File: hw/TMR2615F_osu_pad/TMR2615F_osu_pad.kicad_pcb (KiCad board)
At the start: 4 copper layers, 70.1 x 60 mm, 167 parts, among them J1 TYPE-C-31-M-12, J2 TYPE-C-31-M-12, J3 TYPE-C-31-M-12, J4 XY-SH1_0-4A61, J5 Conn_01x10, J6 Conn_01x23, J7 Conn_01x06, J8 Conn_01x04, SW1 SKSGPAE010, SW2 SKSGPAE010, SW3 CPG151101S11-16, SW4 CPG151101S11-16, SW5 CPG151101S11-16, SW6 CPG151101S11-16, SW7 CPG151101S11-16, SW8 CPG151101S11-16, U1 SRV05-4A, U10 AT32F405RBT7-7, U11 TMUX1574RSVR, U12 SK6812MINI-E, U13 TMR2615x, U14 SK6812MINI-E, U15 TMR2615x, U16 SK6812MINI-E, U17 TMR2615x, U18 SK6812MINI-E, U19 TMR2615x, U2 LM66100DCK, U20 SK6812MINI-E, U21 TMR2615x, U22 SK6812MINI-E, U23 TMR2615x, U24 SK6812MINI-E, U3 AP22653W6-7, U4 TPS7A4700, U5 SRV05-4A, U6 SRV05-4A, U7 LM66100DCK, U8 XC6206P332MR, U9 SRV05-4A, X1 X322512MSB4SI

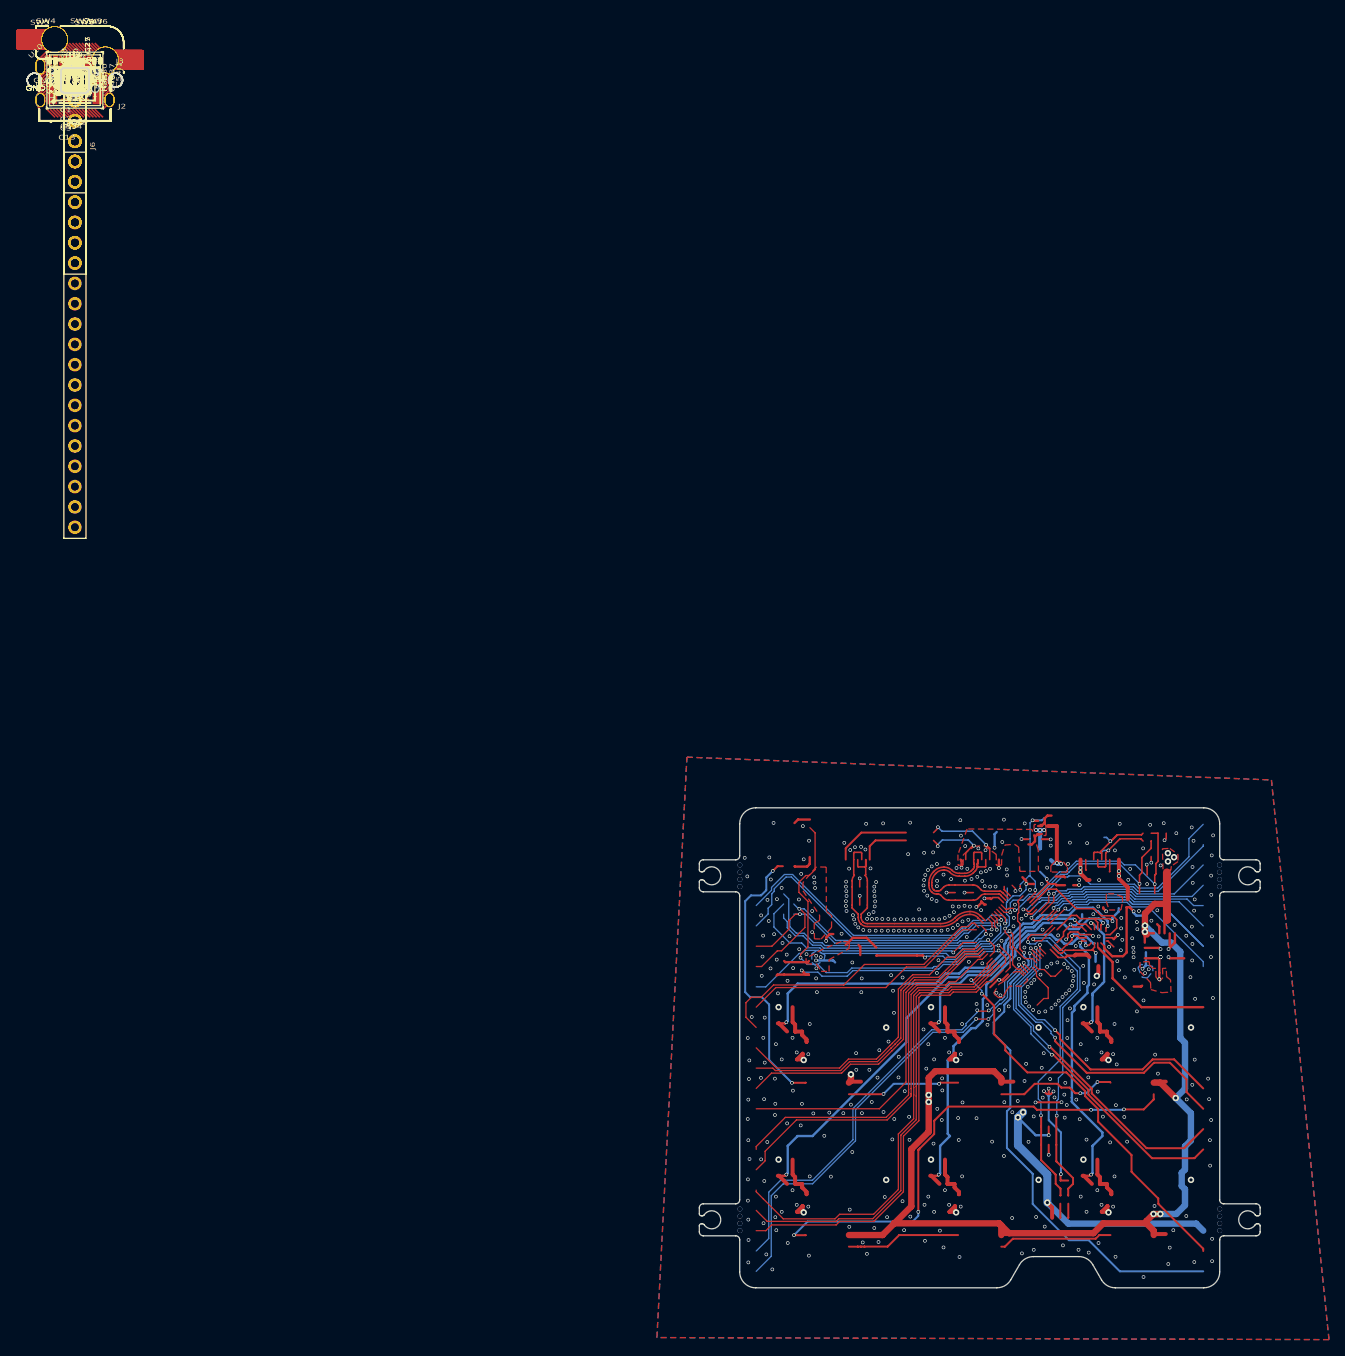
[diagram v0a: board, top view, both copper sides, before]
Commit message: Clear the pre-fab blockers on TMR2615F_osu_pad
All three blockers from prefab_review_2026-08-03.md, plus the should-fix
resistor and a filter retune, in schematic and layout.

U8 XC6206P332MR pinout corrected to the SOT-23 assignment in the LCSC
datasheet — 1=VSS, 2=VOUT, 3=VIN. Pad 2 now carries +3.3V and pad 3 +5V;
before this the +3.3V rail would have come up at ~4.4 V through the pass
device's body diode, past the AT32F405's 4.0 V absolute maximum.

I2C1 SDA and SCL swapped at the MCU so PF4=SDA and PF5=SCL, matching
AT32F405 datasheet Table 9. These pins have no internal remap, so J4's
accessory port had no working hardware I2C before.

U6 (SRV05-4A, SOT-23-6, 3-5 pF per channel and doubled onto each line)
deleted from the USB HS pair and replaced with U25/U26, one
PESD5V0R1BSFYL each on D+ and D-: SOD-962, 0.15 pF, which fits the
~1-2 pF budget at 480 Mbps. The pair was re-dressed around the new
footprints (1789 -> 1766 segments, 628 -> 620 vias). A schematic note
records the fallback: the 0201-class parts can be omitted, or 0402
sub-3 pF diodes fitted on the DNP C17/C18 pads, if assembly balks.

BOOT0 pull-down R26 10 k -> 3.3 k. Table 9 footnote 7 asks for 3.3 kohm
or below.

Sensor and VBUS_B sense filters retuned from 330 ohm + 47 nF to
5.1 kohm + 3.3 nF (R8, R29-R34; C10, C34, C38, C42, C46, C50, C54).
47 nF was over the TMR2615's 10 nF maximum load capacitance; 3.3 nF is
inside it, and the larger series resistor keeps the corner where it was
(tau 16.8 us, f_c 9.46 kHz).

LCSC codes filled in for the three parts the fab BOM could not source
automatically: U2/U7 LM66100DCK = C2869734, U4 TPS7A4700 = C28286.
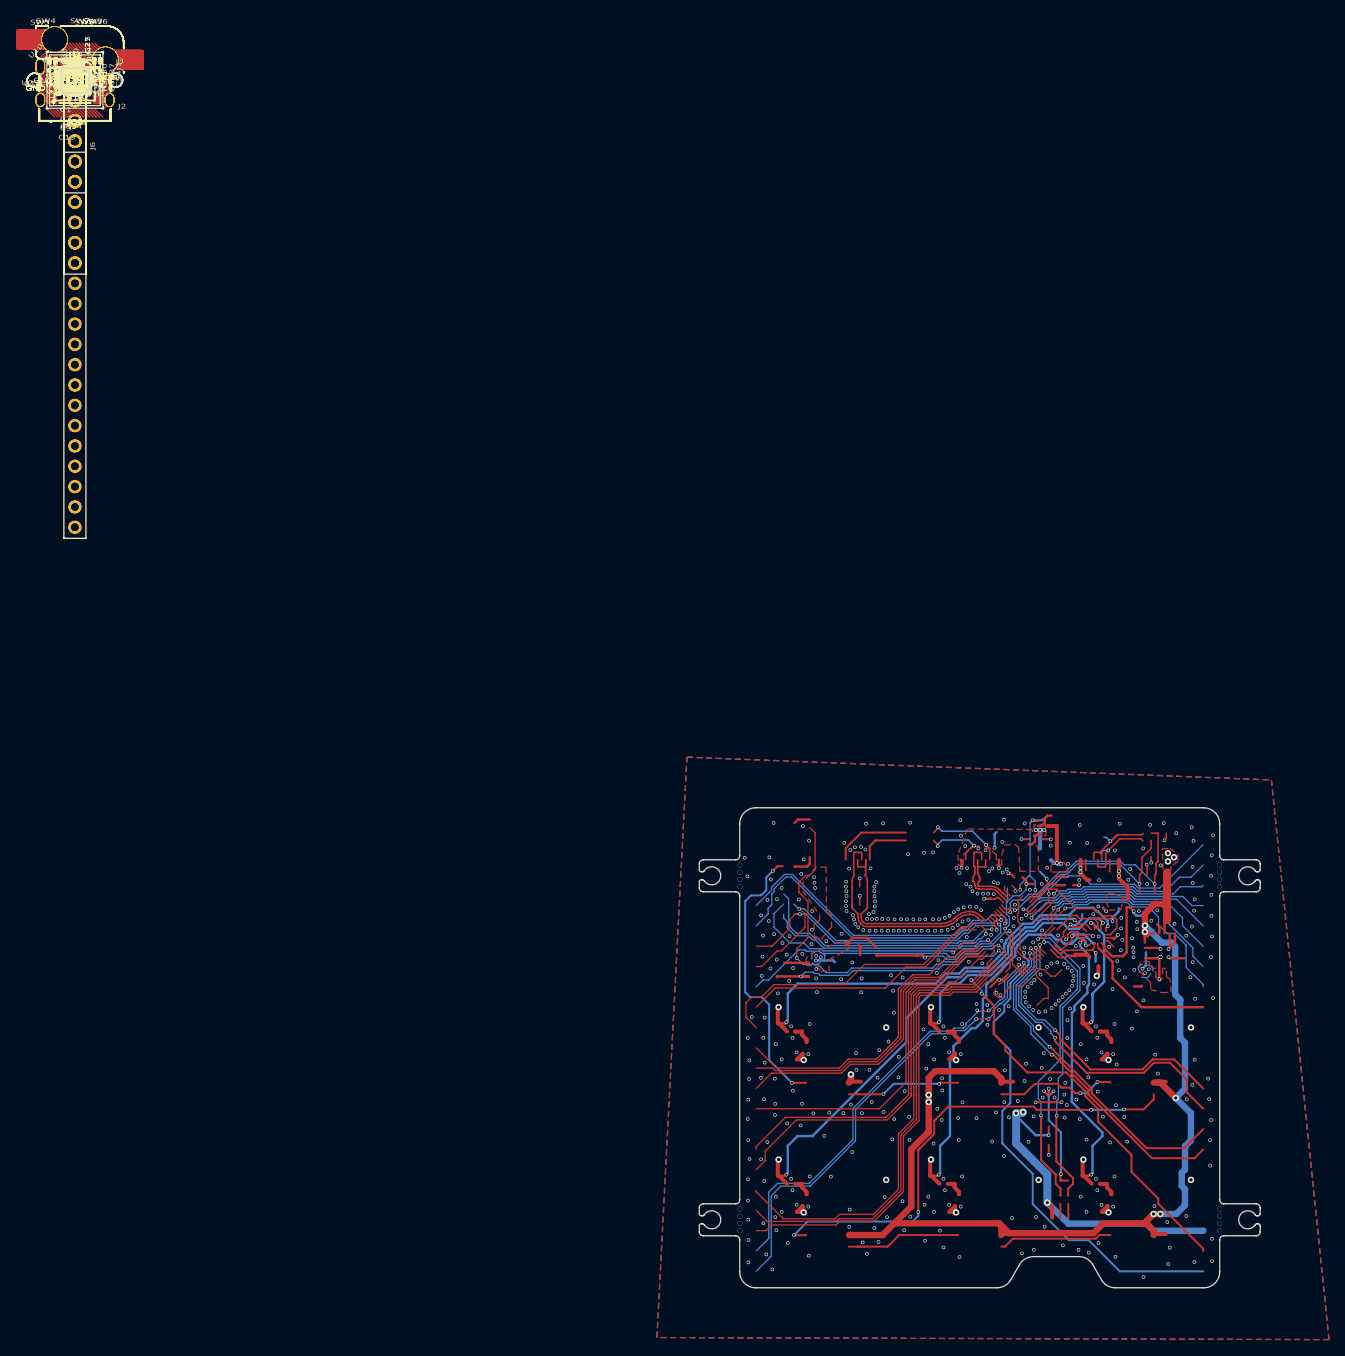
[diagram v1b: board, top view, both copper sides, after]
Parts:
- removed U6: SRV05-4A, Diode__C:SOT-23-6
- added U25, U26: PESD5V0R1BSFYL, Diode__C:SOD-962_L0.6-W0.3-BI, F.Cu at (0.00, 0.00)
- C10, C34, C38, C42, C46, C50, C54: value CL10B473KB8NNNC -> CL10B332KB8NNNC
- R26: value 0402WGF1002TCE -> 0402WGF3301TCE
- R29, R30, R31, R32, R33, R34, R8: value 0402WGF3300TCE -> 0402WGF5101TCE
- U13, U15, U17, U19, U21, U23: value TMR2615x -> TMR2615F-AAC-1.500-500
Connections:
- J5 pad 1: /ADC1_IN15 -> GND
- J5 pad 2: /ADC1_IN14 -> /ADC1_IN15
- J5 pad 3: /ADC1_IN9 -> /ADC1_IN14
- J5 pad 4: /ADC1_IN8 -> /ADC1_IN9
- J5 pad 5: /ADC1_IN7 -> /ADC1_IN8
- J5 pad 6: /ADC1_IN6 -> /ADC1_IN7
- J5 pad 7: /ADC1_IN5 -> /ADC1_IN6
- J5 pad 8: /ADC1_IN4 -> /ADC1_IN5
- J5 pad 9: GND -> /ADC1_IN4
- SW3 pad 2: Net-(U13-VOUT) -> /TMUX_S1A
- SW4 pad 2: Net-(U15-VOUT) -> /TMUX_S1B
- SW5 pad 2: Net-(U17-VOUT) -> /TMUX_S2A
- SW6 pad 2: Net-(U19-VOUT) -> /TMUX_S2B
- SW7 pad 2: Net-(U21-VOUT) -> /TMUX_S3A
- SW8 pad 2: Net-(U23-VOUT) -> /TMUX_S3B
- U10 pad 18: /I2C1_SCL -> /I2C1_SDA
- U10 pad 19: /I2C1_SDA -> /I2C1_SCL
- U8 pad 2: +5V -> +3.3V
- U8 pad 3: +3.3V -> +5V
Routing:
- net +5V: track 254.4 -> 239.4 mm, vias 19 -> 18
- net /OTGHS1_D-: track 22.1 -> 9.57 mm
- net /OTGHS1_D+: track 22.4 -> 10.8 mm
- net /ADC1_IN5: track 39.2 -> 30.6 mm
- net /I2C1_SDA: track 43.5 -> 39.3 mm
- net GND: track 30.9 -> 27.6 mm, vias 473 -> 466
- net Net-(U13-VOUT): track 5.56 -> 2.39 mm, vias 1 -> 0
- net Net-(U21-VOUT): track 5.56 -> 2.39 mm, vias 1 -> 0
- net Net-(U19-VOUT): track 5.56 -> 2.39 mm, vias 1 -> 0
- net Net-(U23-VOUT): track 5.56 -> 2.39 mm, vias 1 -> 0
- net Net-(U15-VOUT): track 5.56 -> 2.39 mm, vias 1 -> 0
- net Net-(U17-VOUT): track 5.56 -> 2.39 mm, vias 1 -> 0
- net /ADC1_IN4: track 24.1 -> 26.9 mm
- net /ADC1_IN15: track 28.5 -> 26.1 mm
- net /TMUX_S2A: track 17.7 -> 19.7 mm, vias 2 -> 3
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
